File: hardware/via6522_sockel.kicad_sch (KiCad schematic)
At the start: 3 parts, among them IC2 VIA6522, P1 VIA_PIN_1-20, P2 VIA_PIN_21-40

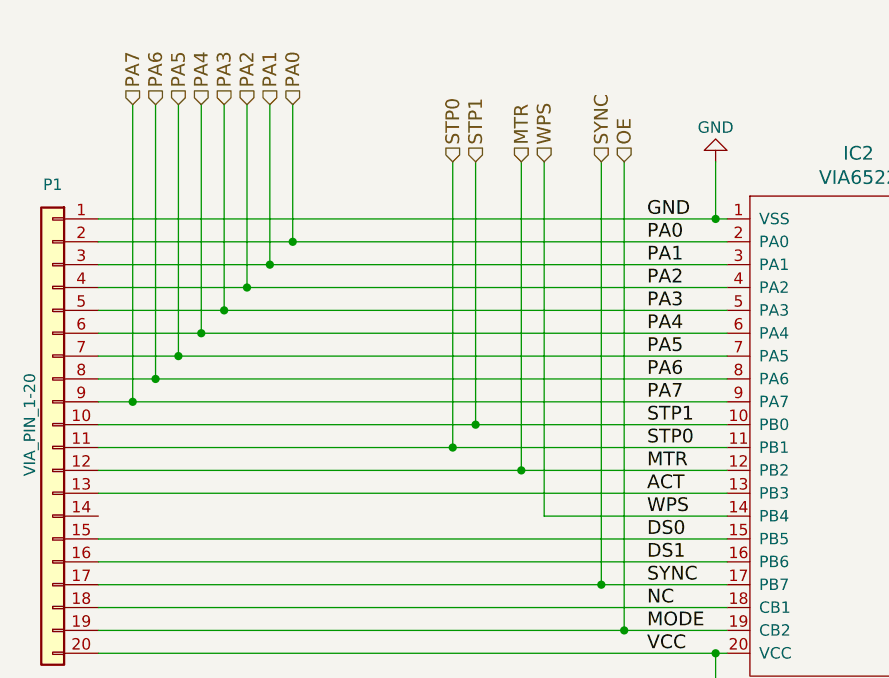
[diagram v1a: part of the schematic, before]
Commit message: new PCB layout to support WPS external
invert WPS signal to be used as input of photo-sensor
circuit of 1541-main pcb.
avoids the concurrent access of the WPS signal between
GateArray and VIA - now this comes from 74LS04
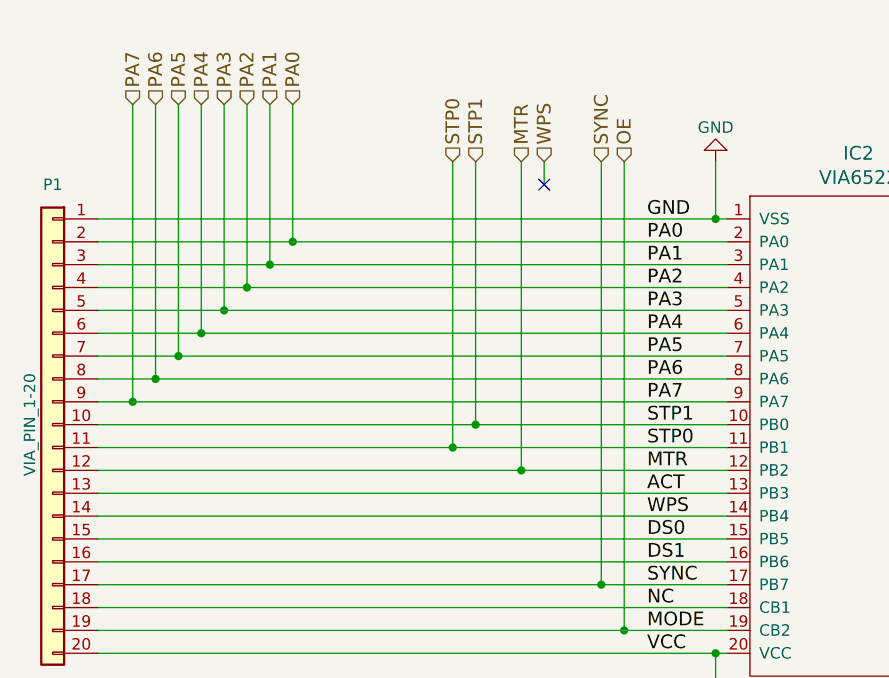
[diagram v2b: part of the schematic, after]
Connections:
- net WPS: now also P1.14 (Pin_14)
- no-connect marks 0 -> 1
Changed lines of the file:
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@@
 		(title "1541-rePico")
 		(date "2026-02-15")
-		(rev "1.3")
+		(rev "1.4")
 	)
 	(junction
@@
 		(color 0 0 0 0)
 	)
+	(no_connect
+		(at 128.27 64.77)
+	)
 	(wire
 		(pts
@@
 	(wire
 		(pts
-			(xy 128.27 62.23) (xy 128.27 101.6)
-		)
-		(stroke
-			(width 0)
-			(type default)
-		)
-	)
-	(wire
-		(pts
 			(xy 95.25 55.88) (xy 95.25 76.2)
 		)
@@
 	(wire
 		(pts
-			(xy 148.59 101.6) (xy 128.27 101.6)
-		)
-		(stroke
-			(width 0)
-			(type default)
-		)
-	)
-	(wire
-		(pts
 			(xy 222.25 93.98) (xy 177.8 93.98)
 		)
@@
 	(wire
 		(pts
+			(xy 78.74 101.6) (xy 148.59 101.6)
+		)
+		(stroke
+			(width 0)
+			(type default)
+		)
+	)
+	(wire
+		(pts
 			(xy 100.33 71.12) (xy 148.59 71.12)
 		)
@@
 		)
 		(stroke
+			(width 0)
+			(type default)
+		)
+	)
+	(wire
+		(pts
+			(xy 128.27 62.23) (xy 128.27 64.77)
+		)
+		(stroke

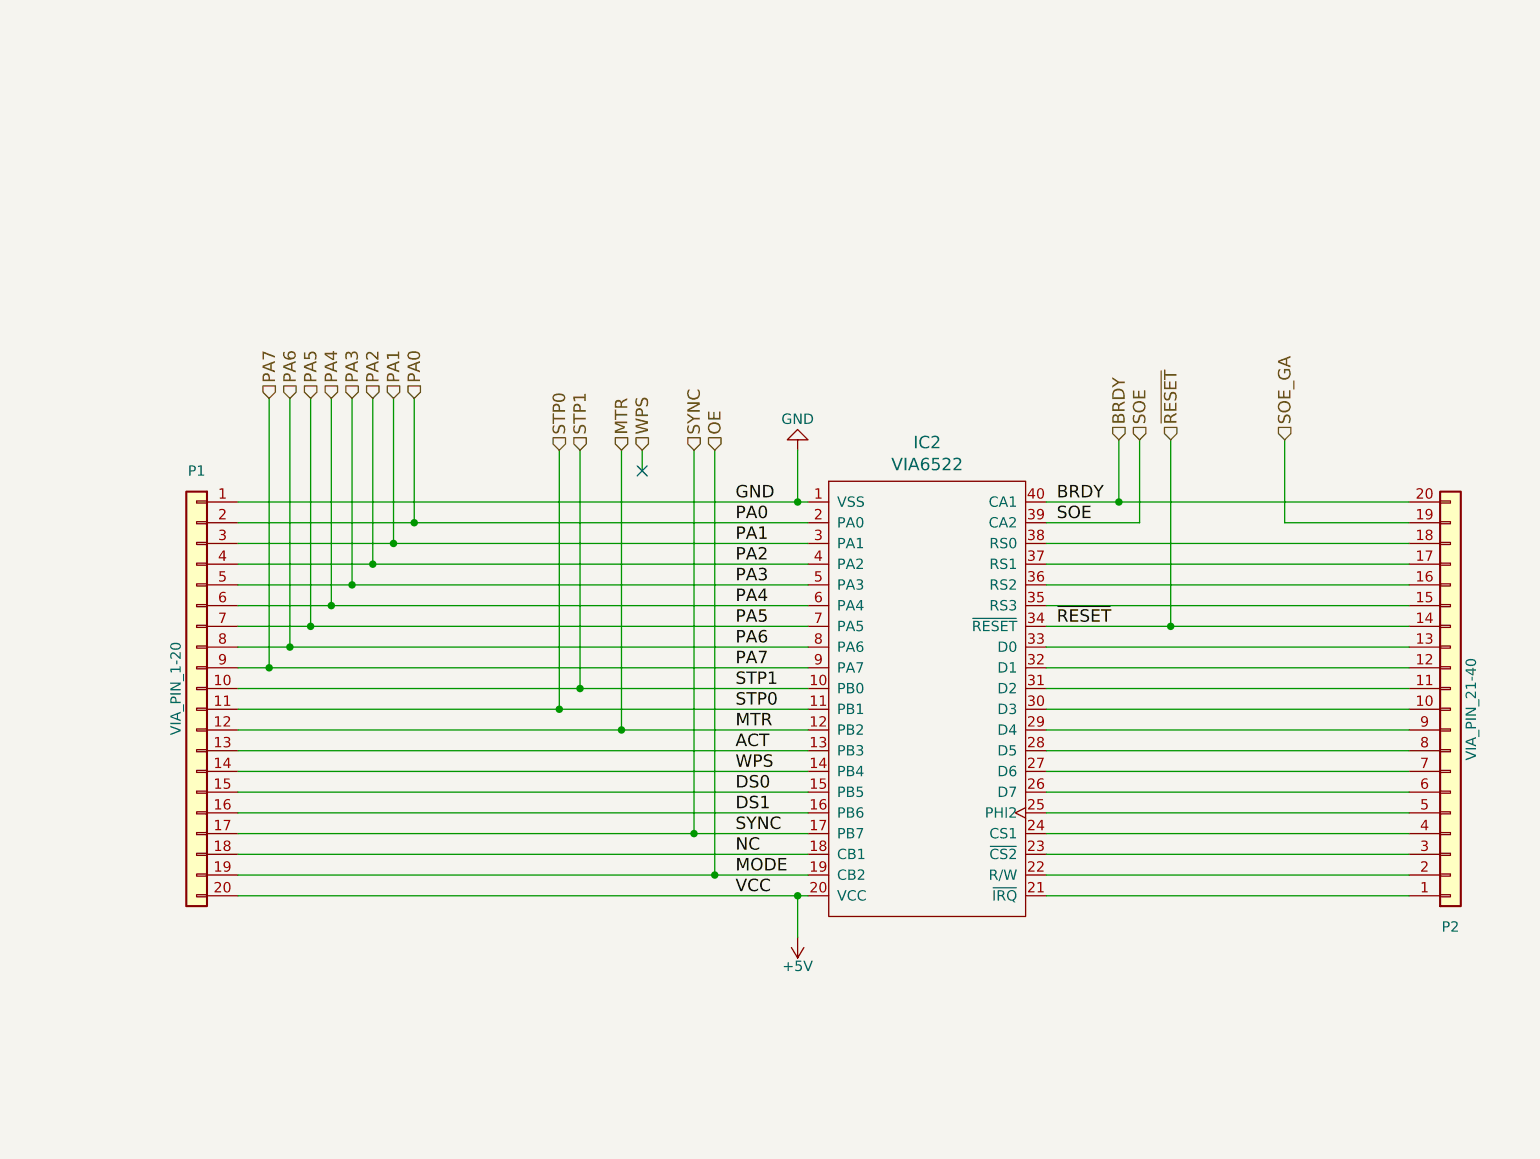
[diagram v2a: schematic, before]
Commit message: new PCB version 1.5
- added levelshifter ics txs0108epwr between pico and via pins
- added pullup-resistors for I2C (populate if necessary)
- aligned footprint of jumper-headers on 50mil grid
- added version-text and URL on backside
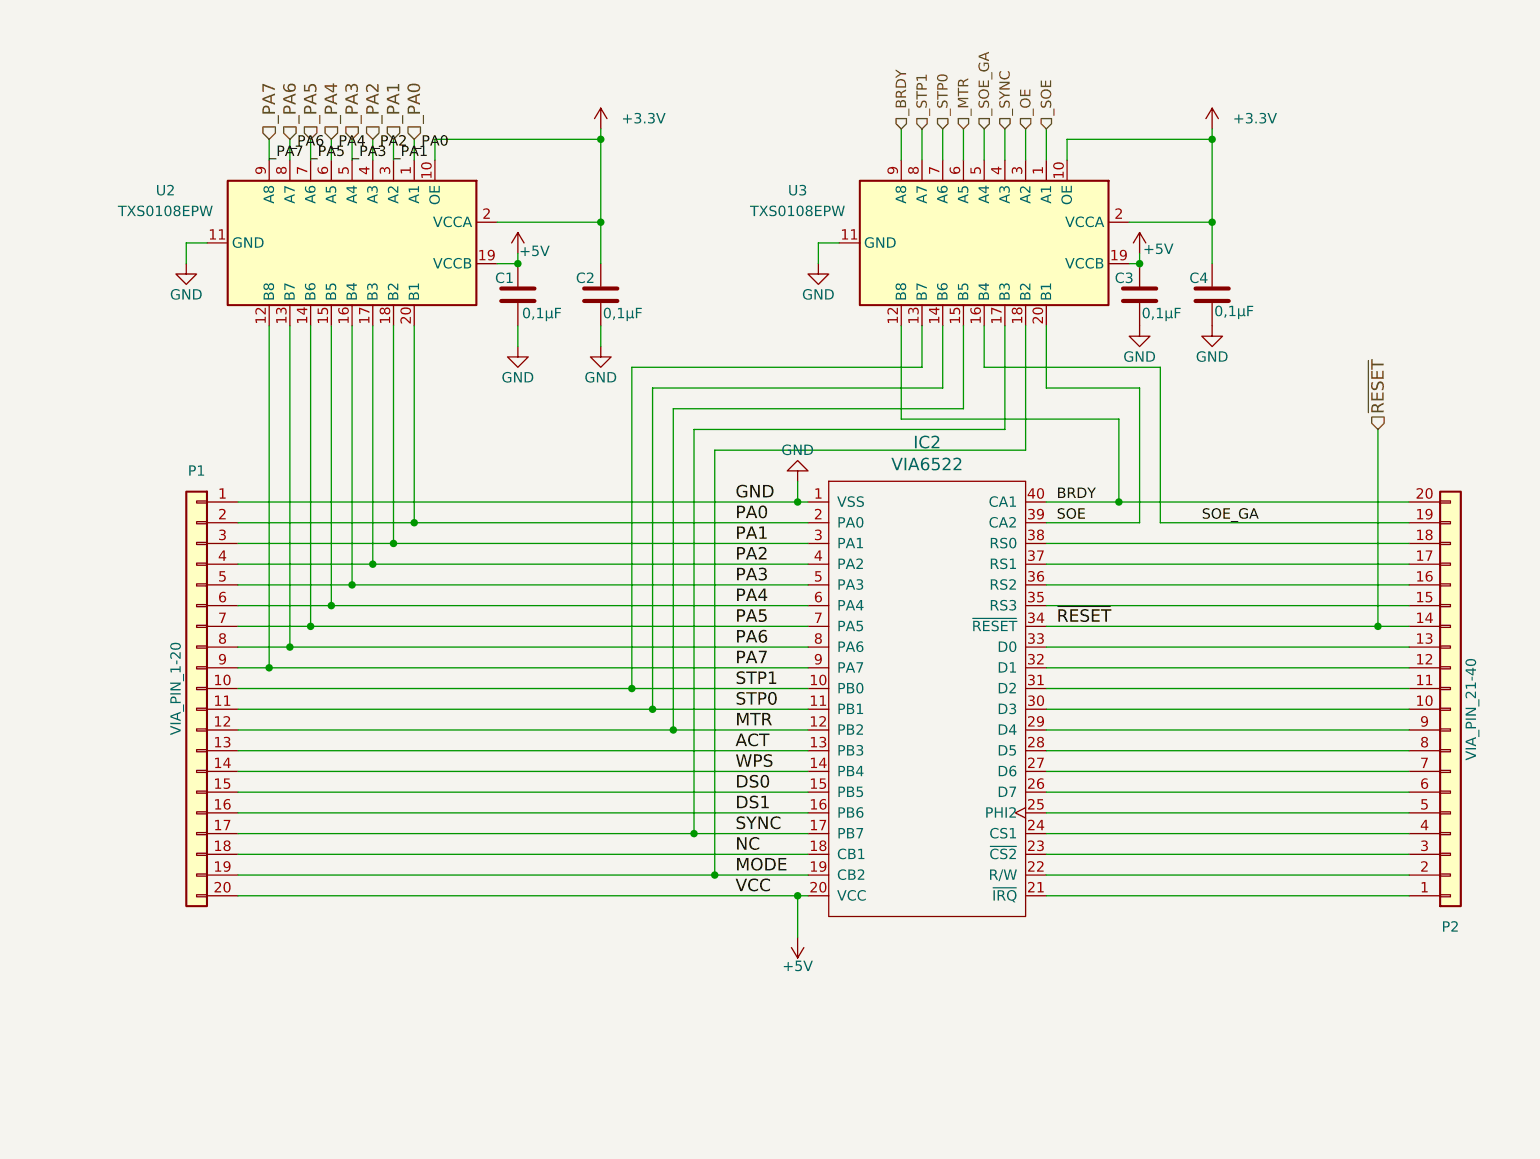
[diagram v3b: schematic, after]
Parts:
- added C1, C2, C3, C4: 0,1µF, Capacitor_SMD:C_0603_1608Metric, symbol Device:C
- added U2, U3: TXS0108EPW, Package_SO:TSSOP-20_4.4x6.5mm_P0.65mm, symbol Logic_LevelTranslator:TXS0108EPW
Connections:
- net +5V: now also C1.1, C3.1, U2.19 (VCCB), U3.19 (VCCB)
- net BRDY: now also U3.12 (B8)
- net GND: now also C1.2, C2.2, C3.2, C4.2, U2.11 (GND), U3.11 (GND)
- net MTR: now also U3.15 (B5)
- net PA0: now also U2.20 (B1)
- net PA1: now also U2.18 (B2)
- net PA2: now also U2.17 (B3)
- net PA3: now also U2.16 (B4)
- net PA4: now also U2.15 (B5)
- net PA5: now also U2.14 (B6)
- net PA6: now also U2.13 (B7)
- net PA7: now also U2.12 (B8)
- net SOE: now also U3.20 (B1)
- net SOE_GA: now also U3.16 (B4)
- net STP0: now also U3.14 (B6)
- net STP1: now also U3.13 (B7)
- net SYNC: now also U3.17 (B3)
- net OE renamed MODE
- net MODE: now also U3.18 (B2)
- new net +3.3V: C2.1, C4.1, U2.10 (OE), U2.2 (VCCA), U3.10 (OE), U3.2 (VCCA)
- new net _BRDY: U3.9 (A8)
- new net _MTR: U3.6 (A5)
- new net _OE: U3.3 (A2)
- new net _PA0: U2.1 (A1)
- new net _PA1: U2.3 (A2)
- new net _PA2: U2.4 (A3)
- new net _PA3: U2.5 (A4)
- new net _PA4: U2.6 (A5)
- new net _PA5: U2.7 (A6)
- new net _PA6: U2.8 (A7)
- new net _PA7: U2.9 (A8)
- new net _SOE: U3.1 (A1)
- new net _SOE_GA: U3.5 (A4)
- new net _STP0: U3.7 (A6)
- new net _STP1: U3.8 (A7)
- new net _SYNC: U3.4 (A3)
- no-connect marks 1 -> 0

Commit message: PCB version 1.6
- use of SN74LVC4245A for levelshifting of PortB-Signals
-> needed an inverted Mode/OE signal for DIR (done via BSS138)
- use of BSS138 for shifting of basic signals (MTR, STP,...)
- cut off "mode/OE" pin from Gatearray -> tied to GND to not let it drive PortB
- rerouted the PCB again -> alignment of Pinheaders and vias
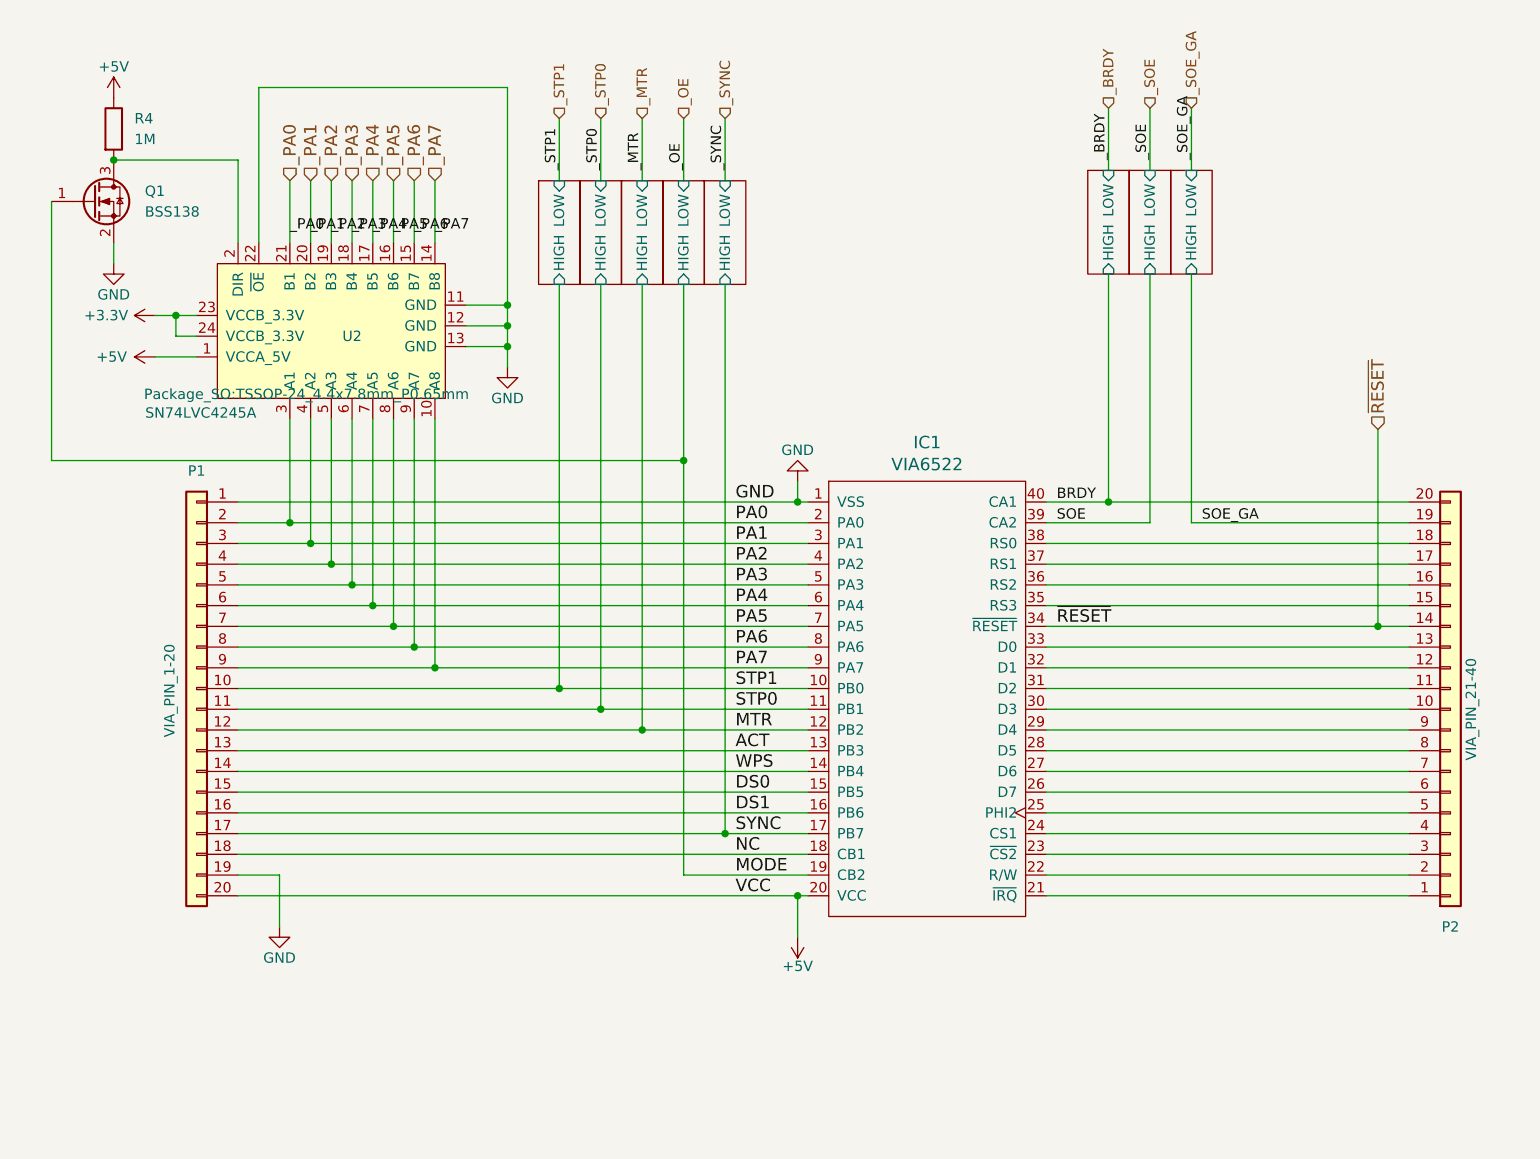
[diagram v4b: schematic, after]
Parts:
- removed C1, C2, C3, C4: 0,1µF, Capacitor_SMD:C_0603_1608Metric, symbol Device:C
- removed U2, U3: TXS0108EPW, Package_SO:TSSOP-20_4.4x6.5mm_P0.65mm, symbol Logic_LevelTranslator:TXS0108EPW
- added Q1: BSS138, Package_TO_SOT_SMD:SOT-23, symbol Transistor_FET:BSS138
- added R4: 1M, Resistor_SMD:R_0603_1608Metric, symbol Device:R
- added U2: SN74LVC4245A, Package_SO:TSSOP-24_4.4x7.8mm_P0.65mm, symbol SN74LVC4245A:SN74LVC4245A
- renumbered IC2 to IC1
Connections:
- net +3.3V: now also U2.23 (VCCB_3.3V), U2.24 (VCCB_3.3V)
- net +5V: now also R4.1, U2.1 (VCCA_5V)
- net GND: now also P1.19 (Pin_19), Q1.2 (S), U2.11 (GND), U2.12 (GND), U2.13 (GND), U2.22 (~{OE})
- net MODE: now also Q1.1 (G); no longer P1.19 (Pin_19)
- net PA0: now also U2.3 (A1)
- net PA1: now also U2.4 (A2)
- net PA2: now also U2.5 (A3)
- net PA3: now also U2.6 (A4)
- net PA4: now also U2.7 (A5)
- net PA5: now also U2.8 (A6)
- net PA6: now also U2.9 (A7)
- net PA7: now also U2.10 (A8)
- net _PA0: now also U2.21 (B1)
- net _PA1: now also U2.20 (B2)
- net _PA2: now also U2.19 (B3)
- net _PA3: now also U2.18 (B4)
- net _PA4: now also U2.17 (B5)
- net _PA5: now also U2.16 (B6)
- net _PA6: now also U2.15 (B7)
- net _PA7: now also U2.14 (B8)
- new net: Q1.3 (D), R4.2, U2.2 (DIR)
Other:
- added sheet BSS138_1 (bss138.kicad_sch)
- added sheet BSS138_2 (bss138.kicad_sch)
- added sheet BSS138_3 (bss138.kicad_sch)
- added sheet BSS138_4 (bss138.kicad_sch)
- added sheet BSS138_5 (bss138.kicad_sch)
- added sheet BSS138_6 (bss138.kicad_sch)
- added sheet BSS138_7 (bss138.kicad_sch)
- added sheet BSS138_8 (bss138.kicad_sch)

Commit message: updated PDFs for PCB v1.6
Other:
- moved on the sheet: IC1, P1, P2, Q1, R4, U2
